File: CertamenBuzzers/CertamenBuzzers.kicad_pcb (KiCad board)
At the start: 2 copper layers, 89.5 x 77.4 mm, 63 parts, among them J1 USB_C_Receptacle_USB2.0_14P, J10 C4, J11 B4, J12 A4, J14 C1, J2 B1, J3 A1, J4 C2, J5 B2, J6 A2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

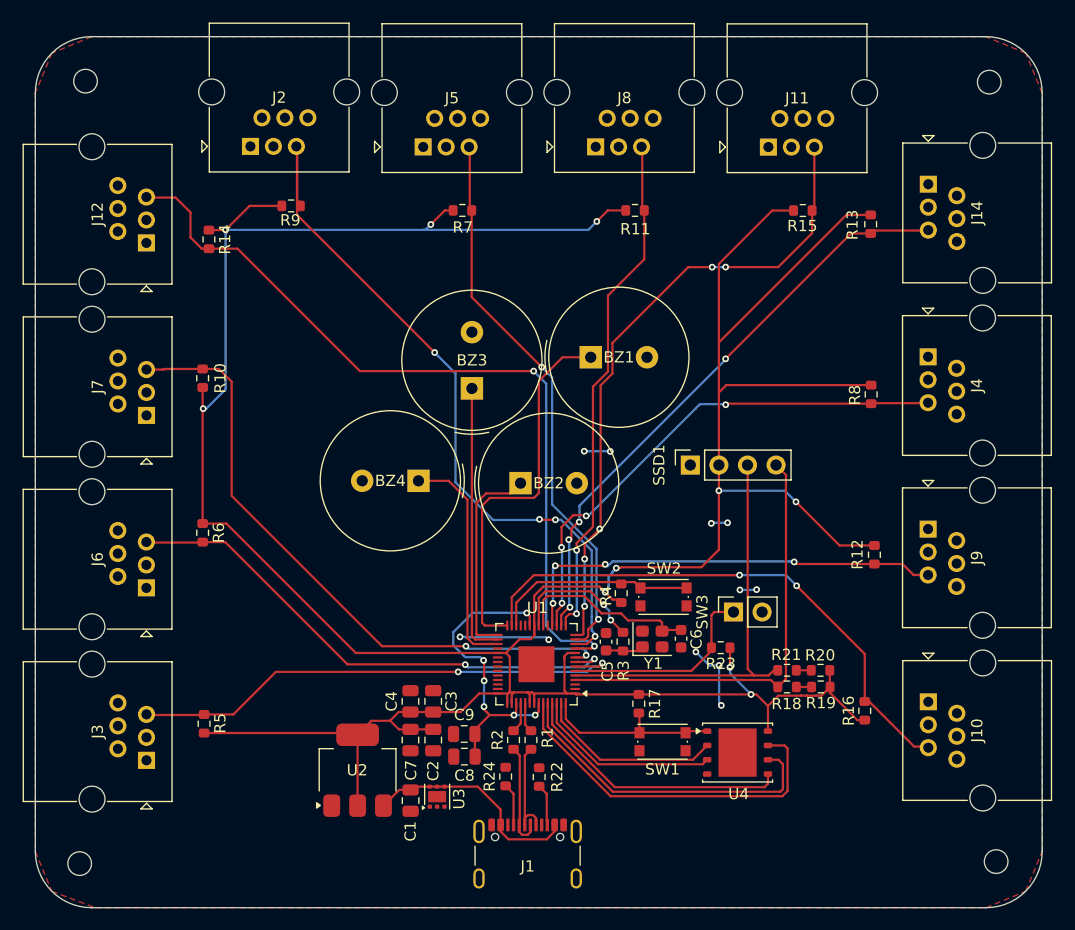
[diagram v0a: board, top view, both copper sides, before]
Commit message: pcb holes realigned
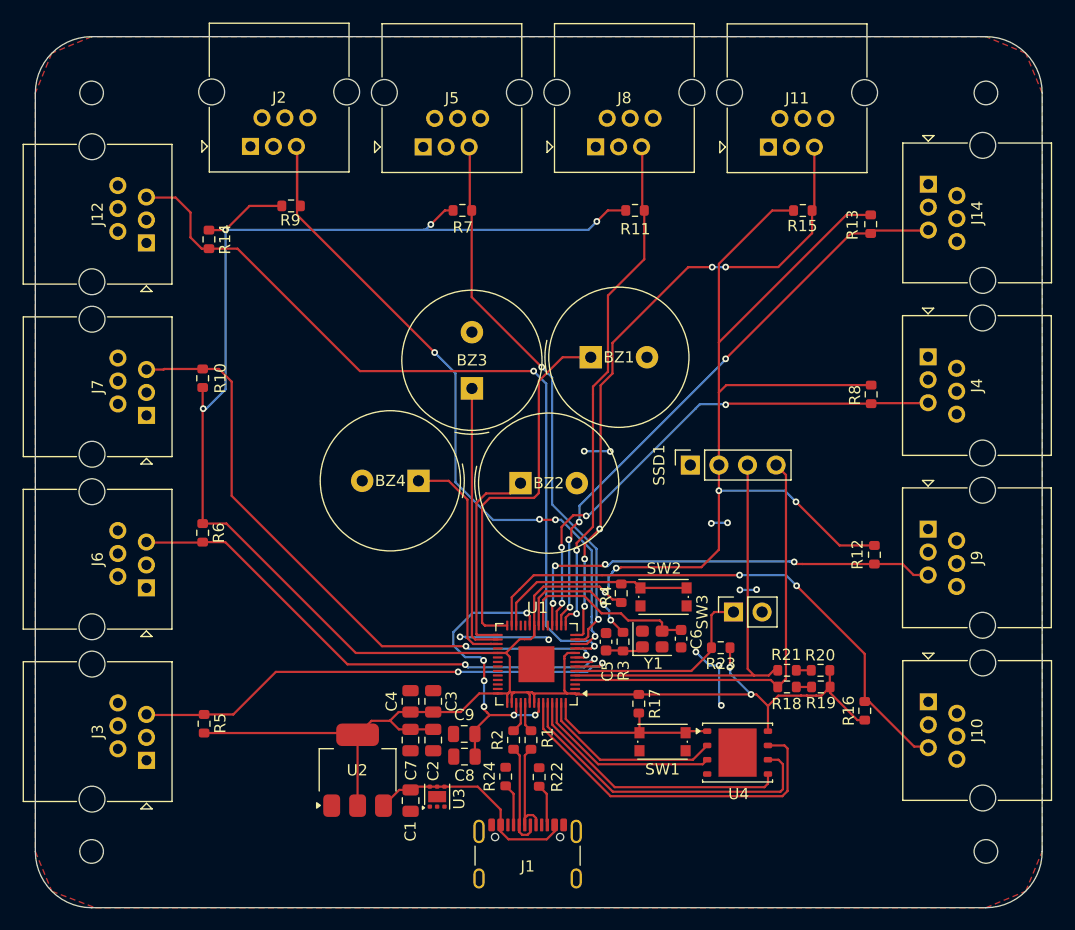
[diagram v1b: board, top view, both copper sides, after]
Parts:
- moved REF** 1.51 mm to (81.3, 143.0)
- moved REF** 1.28 mm to (160.8, 143.0)
- moved REF** 1.18 mm to (81.3, 75.6)
- moved REF** 1.01 mm to (160.8, 75.6)
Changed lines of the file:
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@@
 	(footprint "MountingHole:MountingHole_2.1mm"
 		(layer "F.Cu")
-		(at 161.71 143.89)
+		(at 160.8 142.99)
 		(descr "Mounting Hole 2.1mm, no annular, generated by kicad-footprint-generator mountinghole.py")
 		(tags "mountinghole")
@@
 	(footprint "MountingHole:MountingHole_2.1mm"
 		(layer "F.Cu")
-		(at 80.78 74.53)
+		(at 81.32 75.58)
 		(descr "Mounting Hole 2.1mm, no annular, generated by kicad-footprint-generator mountinghole.py")
 		(tags "mountinghole")
@@
 	(footprint "MountingHole:MountingHole_2.1mm"
 		(layer "F.Cu")
-		(at 80.26 144.07)
+		(at 81.32 142.99)
 		(descr "Mounting Hole 2.1mm, no annular, generated by kicad-footprint-generator mountinghole.py")
 		(tags "mountinghole")
@@
 	(footprint "MountingHole:MountingHole_2.1mm"
 		(layer "F.Cu")
-		(at 161.1 74.62)
+		(at 160.8 75.58)
 		(descr "Mounting Hole 2.1mm, no annular, generated by kicad-footprint-generator mountinghole.py")
 		(tags "mountinghole")

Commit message: buzzer buttons
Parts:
- removed REF** (x4): MountingHole_2.1mm, MountingHole:MountingHole_2.1mm
- added R25: 10k, Resistor_SMD:R_0603_1608Metric, F.Cu at (145.4, 132.8)
- added R26: 10k, Resistor_SMD:R_0603_1608Metric, F.Cu at (127.3, 141.1)
- added R27: 10k, Resistor_SMD:R_0603_1608Metric, F.Cu at (108.8, 121.9)
- added SW4: Score_{A}, Connector_PinSocket_2.54mm:PinSocket_1x02_P2.54mm_Vertical, F.Cu at (148.0, 135.6)
- added SW5: Score_{A}, Connector_PinSocket_2.54mm:PinSocket_1x02_P2.54mm_Vertical, F.Cu at (132.7, 140.9)
- added SW6: Score_{A}, Connector_PinSocket_2.54mm:PinSocket_1x02_P2.54mm_Vertical, F.Cu at (107.2, 119.2)
- moved R17 1.04 mm to (130.7, 130.6), turned to 180 degrees
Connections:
- U1 pad 2: unconnected-(U1-GPIO0-Pad2) -> /Sc_{B}
- U1 pad 3: unconnected-(U1-GPIO1-Pad3) -> /Sc_{A}
- U1 pad 40: unconnected-(U1-GPIO28_ADC2-Pad40) -> /Sc_{C}
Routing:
- net +3V3: track 312.4 -> 349.4 mm, vias 10 -> 12
- net /Sc_{A}: track 0.00 -> 27.4 mm, vias 0 -> 1
- net /Sc_{B}: track 0.00 -> 20.8 mm, vias 0 -> 1
- net /Sc_{C}: track 0.00 -> 16.2 mm, vias 0 -> 2
- net GND: track 19.5 -> 15.8 mm, vias 11 -> 10
- net /A2: track 46.7 -> 49.1 mm
- net /A3: track 56.9 -> 56.4 mm

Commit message: code button stuff
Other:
- board text added: "Stuyvesant Classics & Certamen"
- board text added: "asadpetwalker '27"
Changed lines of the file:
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@@
 		(layer "Edge.Cuts")
+	)
+	(gr_text "Stuyvesant Classics & Certamen"
+		(at 82.25 146.27 0)
+		(layer "F.SilkS" knockout)
+		(effects
+			(font
+				(size 1 1)
+				(thickness 0.25)
+				(bold yes)
+			)
+			(justify left bottom)
+		)
+	)
+	(gr_text "asadpetwalker '27\n"
+		(at 143.93 146.22 0)
+		(layer "F.SilkS" knockout)
+		(effects
+			(font
+				(size 1 1)
+				(thickness 0.25)
+				(bold yes)
+			)
+			(justify left bottom)
+		)
 	)
 	(segment
